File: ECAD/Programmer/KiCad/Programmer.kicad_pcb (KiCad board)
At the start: 2 copper layers, 35.6 x 67.9 mm, 51 parts, among them J1 USB_B_Micro, J2 ARM_SWD, J3 Prog, SW1 POWER VIA USB, U1 FT232RL, U2 STM32F105R8Tx, U3 74HCT245PWR, U4 74HCT245PWR, U5 TPS63030DSK

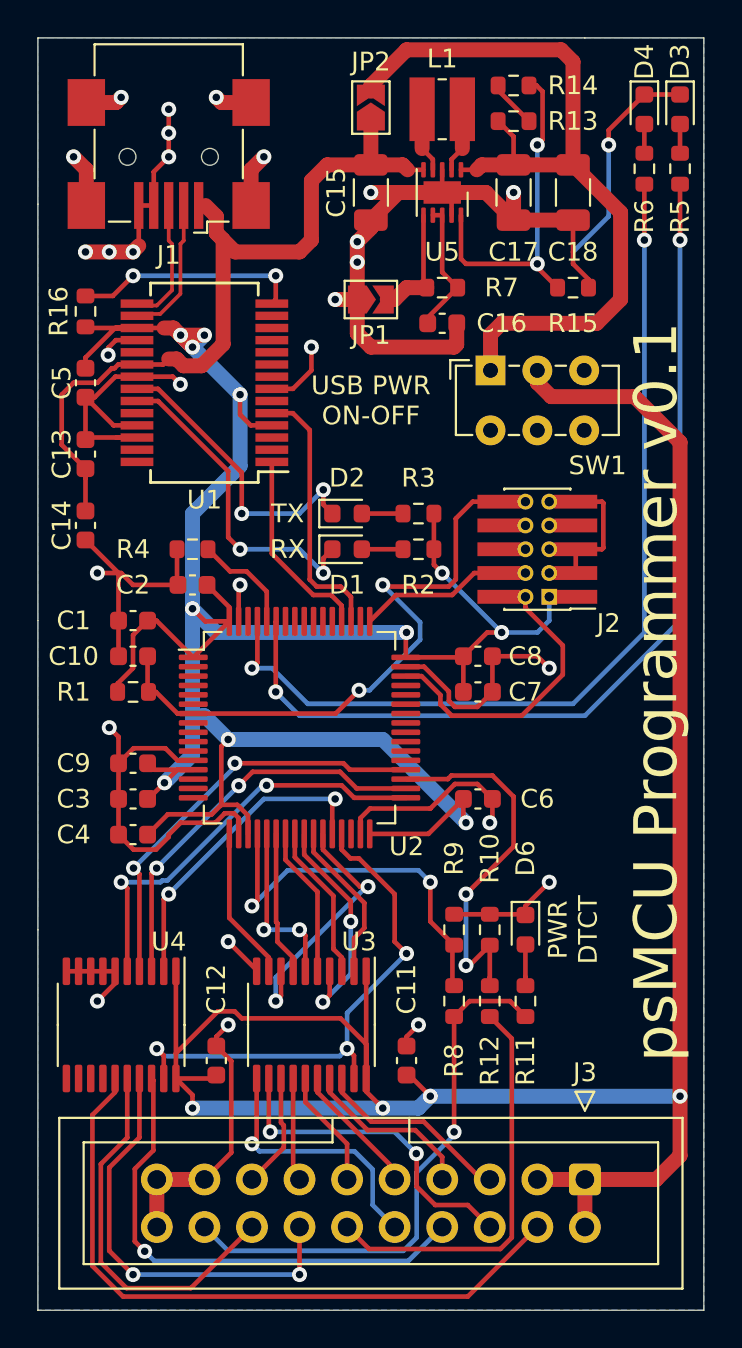
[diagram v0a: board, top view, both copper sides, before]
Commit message: Changed Programmer to differnet STM32
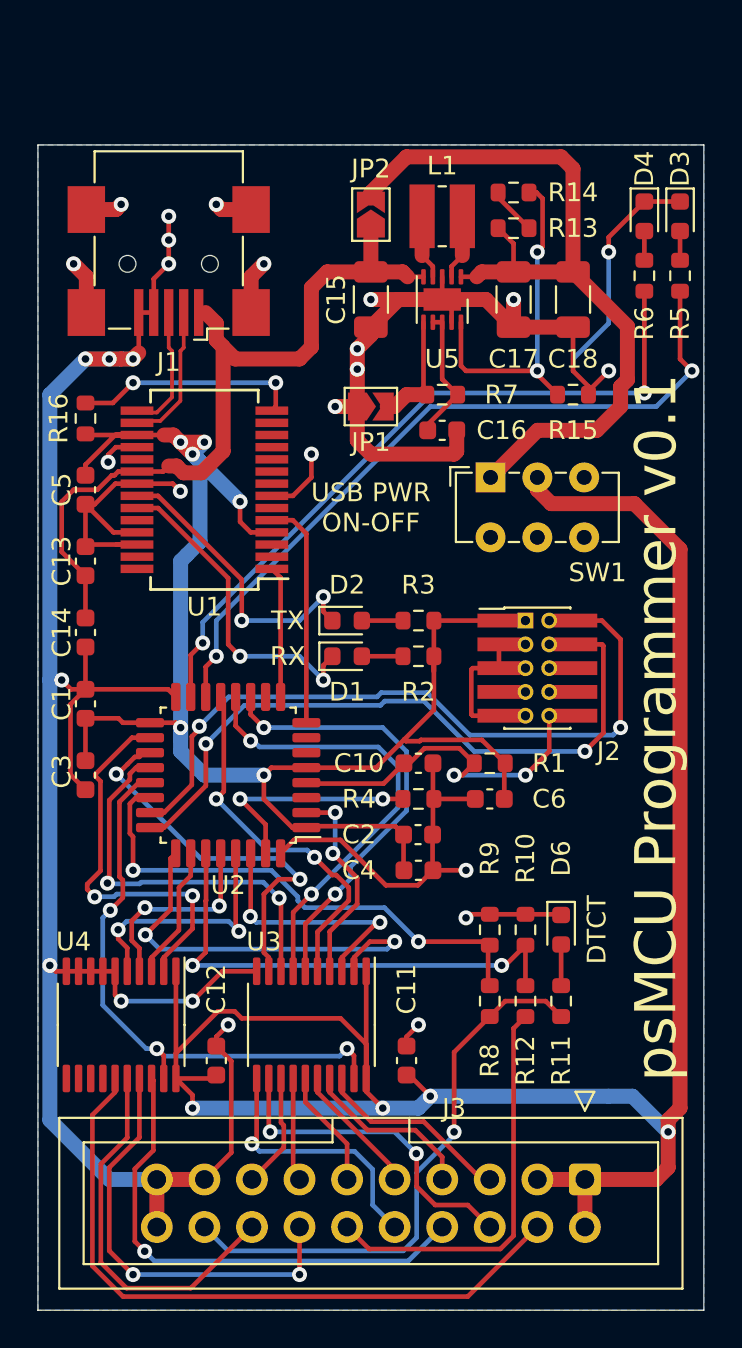
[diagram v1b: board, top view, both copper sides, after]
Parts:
- removed C7: 0u1, Capacitor_SMD:C_0603_1608Metric
- removed C8, C9: 1u, Capacitor_SMD:C_0603_1608Metric
- C1: value 0u1 -> 10n
- C2: value 0u1 -> 1u
- C4: value 0u1 -> 4u7
- U2: value STM32F105R8Tx -> STM32F030K6Tx; footprint Package_QFP:LQFP-64_10x10mm_P0.5mm -> Package_QFP:LQFP-32_7x7mm_P0.8mm
- moved R1 19.4 mm to (153.7, 99.7), turned to 180 degrees
- moved R4 18.0 mm to (149.9, 101.6), turned to 0 degrees
- moved C2 18.0 mm to (149.8, 103.5), turned to 0 degrees
- moved C10 16.3 mm to (149.9, 99.7), turned to 0 degrees
- moved C4 15.4 mm to (149.9, 105.4), turned to 0 degrees
- moved J2 6.35 mm to (156.2, 94.6), turned to 0 degrees
- moved C13 5.72 mm to (132.1, 88.9)
- moved C15 5.72 mm to (147.3, 74.9)
- moved C16 5.72 mm to (151.1, 81.9)
- moved C17 5.72 mm to (154.9, 74.9)
- moved C18 5.72 mm to (158.1, 74.9)
- moved C5 5.72 mm to (132.1, 85.1)
- moved D1 5.72 mm to (146.1, 94.0)
- moved D2 5.72 mm to (146.1, 92.1)
- moved D3 5.72 mm to (163.8, 70.5)
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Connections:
- U2 pad 11: (no net) -> /LV_W_SCLK
- U2 pad 12: GND -> /LV_W_RCLK
- U2 pad 13: +3V3 -> /LV_W_SER
- U2 pad 14: (no net) -> /LED1
- U2 pad 15: (no net) -> /LED2
- U2 pad 16: (no net) -> GND
- U2 pad 17: /LV_DATA_ROM\~PROG~ -> +3V3
- U2 pad 18: GND -> /LV_ADR_~PC~\PROG
- U2 pad 19: +3V3 -> /LV_DATA_ROM\~PROG~
- U2 pad 2: (no net) -> /LV_MEM_~OE
- U2 pad 20: /LV_DTCT_Vtarget -> /LV_DO_RESET
- U2 pad 21: /LV_W_SCLK -> /~5V_OE
- U2 pad 22: /LV_W_RCLK -> /LV_DTCT_Vtarget
- U2 pad 23: /LV_W_SER -> /DIO
- U2 pad 24: /LV_MEM_~PGM -> /CLK
- U2 pad 25: /LV_MEM_~OE -> /LV_MEM_~CE
- U2 pad 26: /LV_MEM_~CE -> /LV_R_SCLK
- U2 pad 27: /LV_DO_RESET -> /LV_R_SER
- U2 pad 28: /LV_ADR_~PC~\PROG -> /LV_R_RCLK
- U2 pad 29: /~5V_OE -> /LV_BKPT_RCLK
- U2 pad 30: (no net) -> /LV_MEM_~PGM
- U2 pad 31: GND -> Net-(R4-Pad1)
- U2 pad 32: +3V3 -> GND
- U2 pad 4: (no net) -> /nRST
- U2 pad 5: (no net) -> +3V3
- U2 pad 7: /nRST -> (no net)
- U2 pad 8: (no net) -> /UART_MCU_TX
- U2 pad 9: (no net) -> /UART_MCU_RX
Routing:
- net +3V3: track 135.8 -> 90.9 mm, vias 11 -> 6
- net GND: track 189.0 -> 225.3 mm, vias 29 -> 28
- net /CLK: track 10.8 -> 37.4 mm, vias 0 -> 2
- net /DIO: track 16.9 -> 39.4 mm, vias 0 -> 2
- net /LV_W_RCLK: track 7.71 -> 24.4 mm, vias 0 -> 2
- net /LV_W_SCLK: track 9.44 -> 24.1 mm
- net /LV_R_SCLK: track 21.4 -> 7.16 mm, vias 2 -> 0
- net /LV_MEM_~CE: track 8.69 -> 22.1 mm, vias 0 -> 2
- net /nRST: track 33.7 -> 20.4 mm
- net /LV_DATA_ROM\~PROG~: track 8.21 -> 20.9 mm, vias 0 -> 2
- net /LV_R_RCLK: track 22.8 -> 10.8 mm
- net /LV_W_SER: track 8.05 -> 19.9 mm, vias 0 -> 2
- net /LED1: track 51.3 -> 39.8 mm
- net /LED2: track 49.9 -> 38.3 mm
- net /LV_BKPT_RCLK: track 22.5 -> 13.5 mm
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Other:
- board size 35.6 x 67.9 mm -> 35.6 x 62.2 mm
- board text added: "DTCT"
- board text removed: "PWR DTCT"

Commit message: First draft v1.0 schematic done, ready for verify
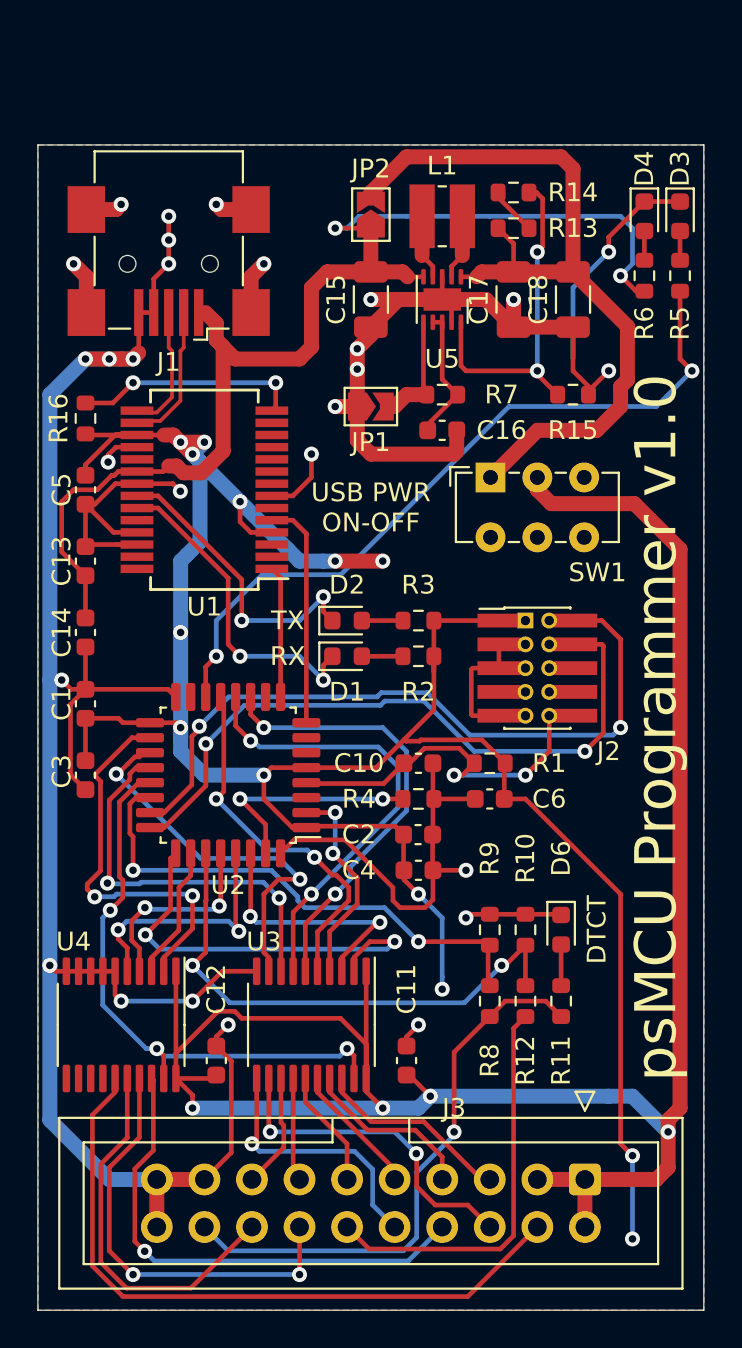
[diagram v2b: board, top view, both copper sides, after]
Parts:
- D3: value LED1 -> LED
- D4: value LED2 -> LED
- R16: value rled -> 10K
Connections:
- R6 pad 1: /LED2 -> /V_USB
- U2 pad 15: /LED2 -> (no net)
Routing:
- net +3V3: track 90.9 -> 134.0 mm, vias 6 -> 13
- net /LED2: track 38.3 -> 0.00 mm, vias 2 -> 0
- net /V_USB: track 42.8 -> 65.5 mm, vias 0 -> 2
- net GND: track 225.3 -> 227.6 mm
- net /LV_R_SER: track 26.7 -> 28.3 mm
- added copper zone on F.Cu, net +3V3
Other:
- board text added: "psMCU Programmer v1.0"
- board text removed: "psMCU Programmer v0.1"

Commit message: Generated Programmer v1.0 production files
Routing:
- net +3V3: track 134.0 -> 167.7 mm, vias 13 -> 14
- net /R_SER: track 21.6 -> 24.5 mm
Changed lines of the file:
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@@
     (thickness 1.6)
     (drawings 10)
-    (tracks 782)
+    (tracks 795)
     (zones 0)
     (modules 48)
@@
   (title_block
     (title Programmer)
-    (date 2021-05-15)
+    (date 2021-05-31)
     (rev v1.0)
     (company "Philipp Schilk")
@@
       (usegerberattributes true)
       (usegerberadvancedattributes true)
-      (creategerberjobfile true)
+      (creategerberjobfile false)
       (excludeedgelayer true)
       (linewidth 0.100000)
@@
       (effects (font (size 1 1) (thickness 0.15)))
     )
-    (fp_text user %R (at 0 0 90) (layer F.Fab)
-      (effects (font (size 0.8 0.8) (thickness 0.12)))
-    )
     (fp_line (start -1.6 0.8) (end -1.6 -0.8) (layer F.Fab) (width 0.1))
     (fp_line (start -1.6 -0.8) (end 1.6 -0.8) (layer F.Fab) (width 0.1))
@@
     (fp_line (start 2.3 -1.15) (end 2.3 1.15) (layer F.CrtYd) (width 0.05))
     (fp_line (start 2.3 1.15) (end -2.3 1.15) (layer F.CrtYd) (width 0.05))
-    (pad 2 smd roundrect (at 1.475 0 90) (size 1.15 1.8) (layers F.Cu F.Paste F.Mask) (roundrect_rratio 0.217391)
+    (fp_text user %R (at 0 0 90) (layer F.Fab)
+      (effects (font (size 0.8 0.8) (thickness 0.12)))
+    )
+    (pad 2 smd roundrect (at 1.475 0 90) (size 1.15 1.8) (layers F.Cu F.Paste F.Mask) (roundrect_rratio 0.2173904347826087)
       (net 53 "Net-(C17-Pad2)"))
-    (pad 1 smd roundrect (at -1.475 0 90) (size 1.15 1.8) (layers F.Cu F.Paste F.Mask) (roundrect_rratio 0.217391)
+    (pad 1 smd roundrect (at -1.475 0 90) (size 1.15 1.8) (layers F.Cu F.Paste F.Mask) (roundrect_rratio 0.2173904347826087)
       (net 3 GND))
     (model ${KISYS3DMOD}/Capacitor_SMD.3dshapes/C_1206_3216Metric.wrl
@@
       (effects (font (size 1 1) (thickness 0.15)))
     )
-    (fp_text user %R (at 0 0 90) (layer F.Fab)
-      (effects (font (size 0.8 0.8) (thickness 0.12)))
-    )
     (fp_line (start -1.6 0.8) (end -1.6 -0.8) (layer F.Fab) (width 0.1))
     (fp_line (start -1.6 -0.8) (end 1.6 -0.8) (layer F.Fab) (width 0.1))
@@
     (fp_line (start 2.3 -1.15) (end 2.3 1.15) (layer F.CrtYd) (width 0.05))
     (fp_line (start 2.3 1.15) (end -2.3 1.15) (layer F.CrtYd) (width 0.05))
-    (pad 2 smd roundrect (at 1.475 0 90) (size 1.15 1.8) (layers F.Cu F.Paste F.Mask) (roundrect_rratio 0.217391)
+    (fp_text user %R (at 0 0 90) (layer F.Fab)
+      (effects (font (size 0.8 0.8) (thickness 0.12)))
+    )
+    (pad 2 smd roundrect (at 1.475 0 90) (size 1.15 1.8) (layers F.Cu F.Paste F.Mask) (roundrect_rratio 0.2173904347826087)
       (net 53 "Net-(C17-Pad2)"))
-    (pad 1 smd roundrect (at -1.475 0 90) (size 1.15 1.8) (layers F.Cu F.Paste F.Mask) (roundrect_rratio 0.217391)
+    (pad 1 smd roundrect (at -1.475 0 90) (size 1.15 1.8) (layers F.Cu F.Paste F.Mask) (roundrect_rratio 0.2173904347826087)
       (net 3 GND))
     (model ${KISYS3DMOD}/Capacitor_SMD.3dshapes/C_1206_3216Metric.wrl
@@
       (effects (font (size 1 1) (thickness 0.15)))
     )
-    (fp_text user %R (at 0 0 90) (layer F.Fab)
-      (effects (font (size 0.8 0.8) (thickness 0.12)))
-    )
     (fp_line (start -1.6 0.8) (end -1.6 -0.8) (layer F.Fab) (width 0.1))
     (fp_line (start -1.6 -0.8) (end 1.6 -0.8) (layer F.Fab) (width 0.1))
@@
     (fp_line (start 2.3 -1.15) (end 2.3 1.15) (layer F.CrtYd) (width 0.05))
     (fp_line (start 2.3 1.15) (end -2.3 1.15) (layer F.CrtYd) (width 0.05))
-    (pad 2 smd roundrect (at 1.475 0 90) (size 1.15 1.8) (layers F.Cu F.Paste F.Mask) (roundrect_rratio 0.217391)
+    (fp_text user %R (at 0 0 90) (layer F.Fab)
+      (effects (font (size 0.8 0.8) (thickness 0.12)))
+    )
+    (pad 2 smd roundrect (at 1.475 0 90) (size 1.15 1.8) (layers F.Cu F.Paste F.Mask) (roundrect_rratio 0.2173904347826087)
       (net 14 /V_USB))
-    (pad 1 smd roundrect (at -1.475 0 90) (size 1.15 1.8) (layers F.Cu F.Paste F.Mask) (roundrect_rratio 0.217391)
+    (pad 1 smd roundrect (at -1.475 0 90) (size 1.15 1.8) (layers F.Cu F.Paste F.Mask) (roundrect_rratio 0.2173904347826087)
       (net 3 GND))
     (model ${KISYS3DMOD}/Capacitor_SMD.3dshapes/C_1206_3216Metric.wrl
@@
   (segment (start 139.790002 112.485002) (end 152.309998 112.485002) (width 0.25) (layer B.Cu) (net 1))
   (segment (start 152.309998 112.485002) (end 154.305 110.49) (width 0.25) (layer B.Cu) (net 1))
-  (segment (start 147.225001 125.635001) (end 146.05 124.46) (width 0.25) (layer F.Cu) (net 2))
   (segment (start 154.234001 125.635001) (end 147.225001 125.635001) (width 0.25) (layer F.Cu) (net 2))
+  (segment (start 147.225001 125.635001) (end 146.05 124.46) (width 0.25) (layer F.Cu) (net 2))
   (segment (start 154.94 124.929002) (end 154.234001 125.635001) (width 0.25) (layer F.Cu) (net 2))
-  (segment (start 154.94 113.855) (end 154.94 124.929002) (width 0.25) (layer F.Cu) (net 2))
-  (segment (start 155.575 113.22) (end 154.94 113.855) (width 0.25) (layer F.Cu) (net 2))
+  (segment (start 154.94 121.285) (end 154.94 124.929002) (width 0.25) (layer F.Cu) (net 2))
+  (segment (start 152.4 118.745) (end 154.94 121.285) (width 0.25) (layer F.Cu) (net 2))
+  (segment (start 153.67 114.3) (end 152.4 115.57) (width 0.25) (layer F.Cu) (net 2))
+  (segment (start 154.895 114.3) (end 153.67 114.3) (width 0.25) (layer F.Cu) (net 2))
+  (segment (start 152.4 115.57) (end 152.4 118.745) (width 0.25) (layer F.Cu) (net 2))
+  (segment (start 155.575 113.62) (end 154.895 114.3) (width 0.25) (layer F.Cu) (net 2))
+  (segment (start 155.575 113.22) (end 155.575 113.62) (width 0.25) (layer F.Cu) (net 2))
   (segment (start 151.13 73.7175) (end 151.13 74.93) (width 0.25) (layer F.Cu) (net 3) (status 30))
   (segment (start 151.63 75.43) (end 151.13 74.93) (width 0.25) (layer F.Cu) (net 3) (status 30))
@@
   (segment (start 137.16 98.425) (end 137.16 92.71) (width 0.8) (layer B.Cu) (net 4))
   (segment (start 137.16 92.71) (end 137.16 88.9) (width 0.8) (layer B.Cu) (net 4))
+  (segment (start 161.29 125.095) (end 161.29 127) (width 0.25) (layer B.Cu) (net 4))
+  (segment (start 161.29 127) (end 160.02 128.27) (width 0.25) (layer B.Cu) (net 4))
+  (segment (start 160.02 128.27) (end 133.35 128.27) (width 0.25) (layer B.Cu) (net 4))
+  (via (at 131.445 125.73) (size 0.8) (drill 0.4) (layers F.Cu B.Cu) (net 4))
+  (segment (start 131.445 126.365) (end 131.445 125.73) (width 0.25) (layer B.Cu) (net 4))
+  (segment (start 133.35 128.27) (end 131.445 126.365) (width 0.25) (layer B.Cu) (net 4))
   (segment (start 149.085 99.695) (end 147.999989 100.780011) (width 0.25) (layer F.Cu) (net 5))
   (segment (start 147.999989 100.780011) (end 143.925011 100.780011) (width 0.25) (layer F.Cu) (net 5))
@@
   (segment (start 137.15 80.3382) (end 137.15 77.675001) (width 0.2) (layer F.Cu) (net 49))
   (segment (start 136.0732 81.415) (end 137.15 80.3382) (width 0.2) (layer F.Cu) (net 49))
-  (segment (start 133.66 117.265) (end 133.66 116.5275) (width 0.25) (layer F.Cu) (net 50) (status 20))
-  (segment (start 132.449978 118.475022) (end 133.66 117.265) (width 0.25) (layer F.Cu) (net 50))
   (segment (start 132.449978 126.539393) (end 132.449978 118.475022) (width 0.25) (layer F.Cu) (net 50))
-  (segment (start 152.494987 128.175013) (end 134.085598 128.175013) (width 0.25) (layer F.Cu) (net 50))
-  (segment (start 156.21 124.46) (end 152.494987 128.175013) (width 0.25) (layer F.Cu) (net 50) (status 10))
+  (segment (start 143.604987 128.175013) (end 134.085598 128.175013) (width 0.25) (layer F.Cu) (net 50))
+  (segment (start 145.694988 126.085012) (end 143.604987 128.175013) (width 0.25) (layer F.Cu) (net 50))
+  (segment (start 133.66 117.265) (end 133.66 116.5275) (width 0.25) (layer F.Cu) (net 50))
   (segment (start 134.085598 128.175013) (end 132.449978 126.539393) (width 0.25) (layer F.Cu) (net 50))
+  (segment (start 154.584988 126.085012) (end 145.694988 126.085012) (width 0.25) (layer F.Cu) (net 50))
+  (segment (start 132.449978 118.475022) (end 133.66 117.265) (width 0.25) (layer F.Cu) (net 50))
+  (segment (start 156.21 124.46) (end 154.584988 126.085012) (width 0.25) (layer F.Cu) (net 50))
   (via (at 133.824815 108.585) (size 0.8) (drill 0.4) (layers F.Cu B.Cu) (net 51))
   (segment (start 134.31 110.8025) (end 134.31 109.554441) (width 0.25) (layer F.Cu) (net 51))
